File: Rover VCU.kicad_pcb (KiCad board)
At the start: 2 copper layers, 8 x 5 mm, 0 parts

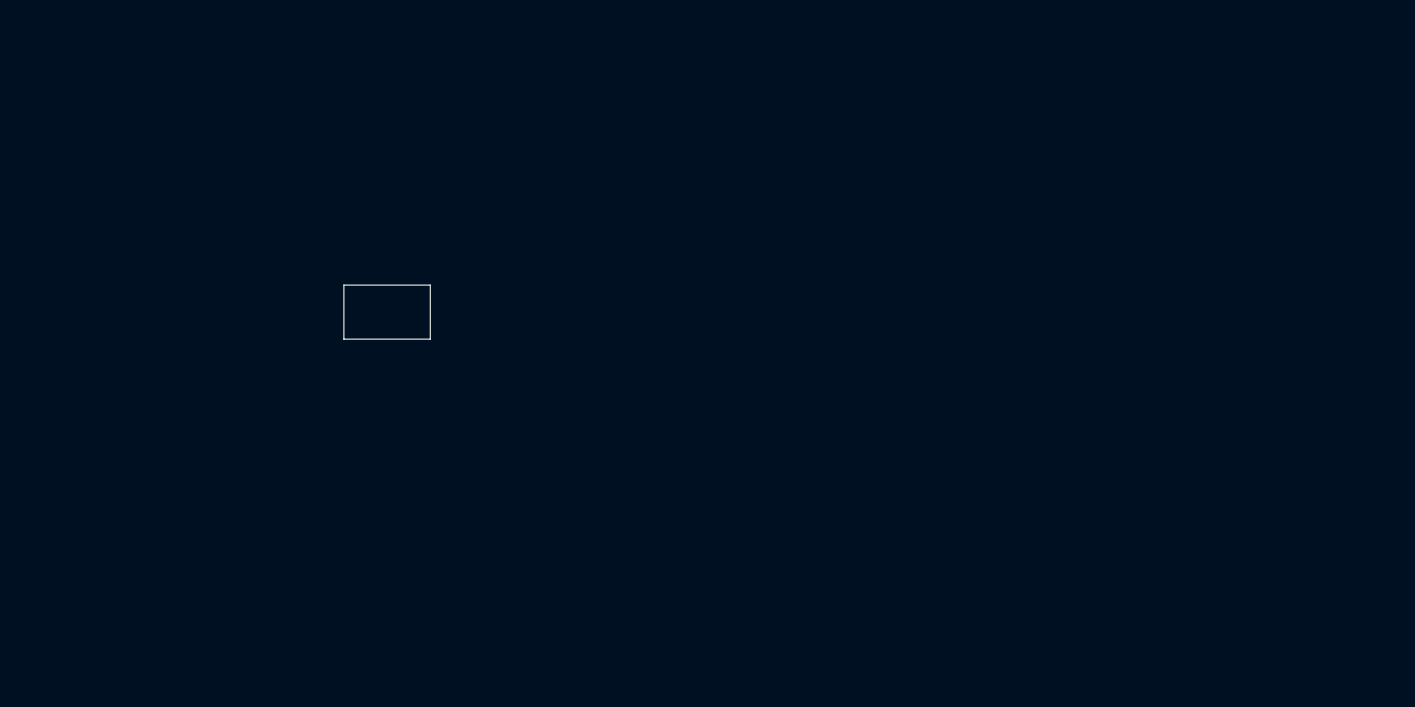
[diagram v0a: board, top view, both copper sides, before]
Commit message: feat: added MVP routing implementation
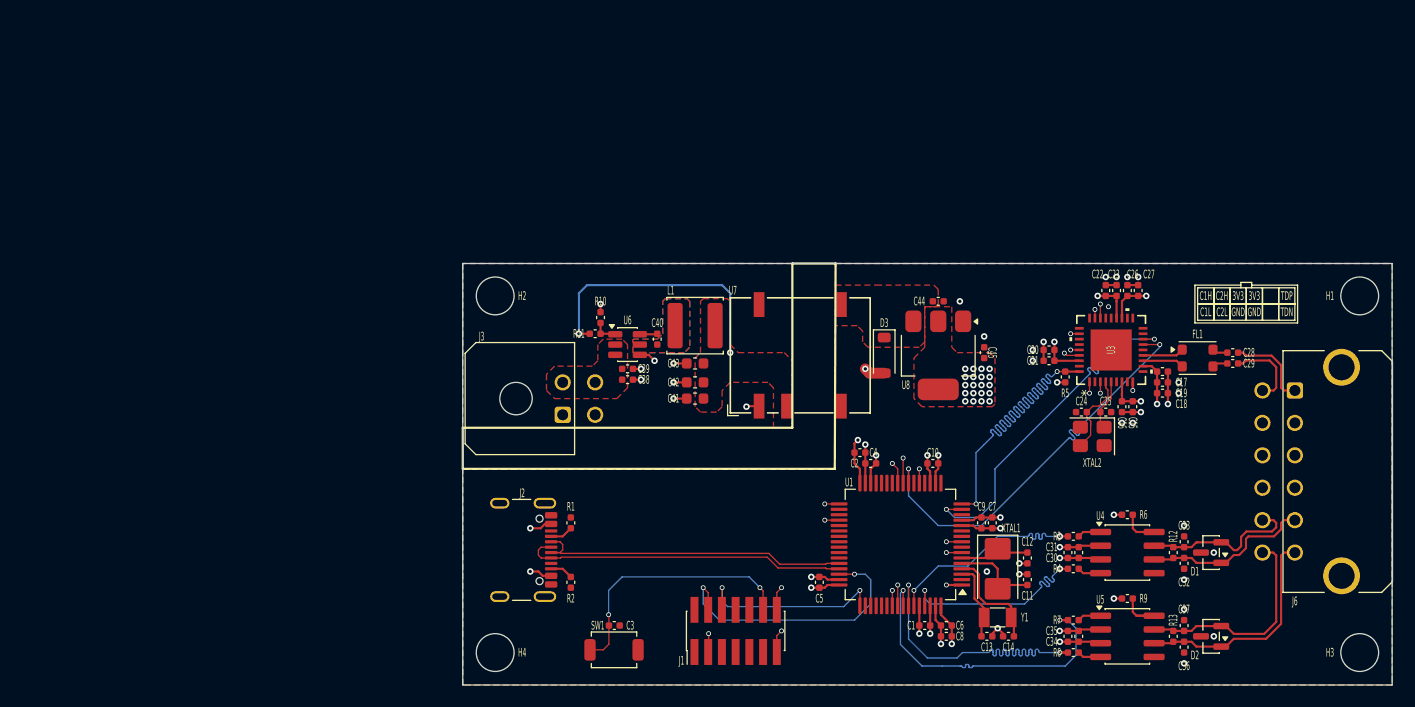
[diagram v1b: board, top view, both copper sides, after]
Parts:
- added C1: 2.2uF, chenry-footprint-lib:C_0402, F.Cu at (182.8, 128.5)
- added C10: 100nF, chenry-footprint-lib:C_0402, F.Cu at (183.5, 113.5)
- added C11: 10pF, chenry-footprint-lib:C_0402, F.Cu at (192.2, 124.2)
- added C12: 10pF, chenry-footprint-lib:C_0402, F.Cu at (192.3, 122.2)
- added C13: 6pF, chenry-footprint-lib:C_0402, F.Cu at (188.5, 129.5)
- added C14: 6pF, chenry-footprint-lib:C_0402, F.Cu at (190.5, 129.5)
- added C15: 100nF, chenry-footprint-lib:C_0402, F.Cu at (202.0, 108.2)
- added C16: 1uF, chenry-footprint-lib:C_0402, F.Cu at (201.0, 108.2)
- added C17: 10nF, chenry-footprint-lib:C_0402, F.Cu at (204.8, 105.0)
- added C18: 470nF, chenry-footprint-lib:C_0402, F.Cu at (204.8, 107.0)
- added C19: 1uF, chenry-footprint-lib:C_0402, F.Cu at (204.8, 106.0)
- added C2: 2.2uF, chenry-footprint-lib:C_0402, F.Cu at (177.8, 113.5)
- added C20: 10nF, chenry-footprint-lib:C_0402, F.Cu at (194.2, 103.0)
- added C21: 1uF, chenry-footprint-lib:C_0402, F.Cu at (194.2, 104.0)
- added C22: 470nF, chenry-footprint-lib:C_0402, F.Cu at (199.5, 97.5)
- added C23: 10nF, chenry-footprint-lib:C_0402, F.Cu at (200.5, 97.5)
- added C24: 22pF, chenry-footprint-lib:C_0402, F.Cu at (197.2, 108.8)
- added C25: 22pF, chenry-footprint-lib:C_0402, F.Cu at (199.5, 108.8)
- added C26: 100nF, chenry-footprint-lib:C_0402, F.Cu at (201.5, 97.5)
- added C27: 2.2uF, chenry-footprint-lib:C_0402, F.Cu at (202.5, 97.5)
- added C28: 100nF, chenry-footprint-lib:C_0402, F.Cu at (211.2, 104.2)
- added C29: 100nF, chenry-footprint-lib:C_0402, F.Cu at (211.2, 103.2)
- added C3: 100nF, chenry-footprint-lib:C_0402, F.Cu at (154.0, 128.5)
- added C30: 4.7uF, chenry-footprint-lib:C_0402, F.Cu at (196.0, 121.8)
- added C31: 100nF, chenry-footprint-lib:C_0402, F.Cu at (197.0, 121.8)
- added C32: 1pF, chenry-footprint-lib:C_0402, F.Cu at (206.8, 122.8)
- added C33: 1pF, chenry-footprint-lib:C_0402, F.Cu at (206.8, 120.8)
- added C34: 4.7uF, chenry-footprint-lib:C_0402, F.Cu at (196.0, 129.5)
- added C35: 100nF, chenry-footprint-lib:C_0402, F.Cu at (197.0, 129.5)
- added C36: 1pF, chenry-footprint-lib:C_0402, F.Cu at (206.8, 130.5)
- added C37: 1pF, chenry-footprint-lib:C_0402, F.Cu at (206.8, 128.5)
- added C38: 100nF, chenry-footprint-lib:C_0402, F.Cu at (155.3, 105.8)
- added C39: 1uF, chenry-footprint-lib:C_0402, F.Cu at (155.2, 104.8)
- added C4: 100nF, chenry-footprint-lib:C_0402, F.Cu at (176.8, 112.5)
- added C40: 100nF, chenry-footprint-lib:C_0402, F.Cu at (158.0, 102.0)
- added C41: 22uF, Capacitor_SMD:C_0603_1608Metric, F.Cu at (161.5, 107.5)
- added C42: 22uF, Capacitor_SMD:C_0603_1608Metric, F.Cu at (161.5, 106.0)
- added C43: 22uF, Capacitor_SMD:C_0603_1608Metric, F.Cu at (161.5, 104.2)
- added C44: 1uF, chenry-footprint-lib:C_0402, F.Cu at (184.0, 98.5)
- added C45: 1uF, chenry-footprint-lib:C_0402, F.Cu at (188.2, 103.2)
- added C5: 100nF, chenry-footprint-lib:C_0402, F.Cu at (173.0, 124.5)
- added C6: 100nF, chenry-footprint-lib:C_0402, F.Cu at (184.8, 128.5)
- added C7: 4.7uF, chenry-footprint-lib:C_0402, F.Cu at (189.0, 119.0)
- added C8: 4.7uF, chenry-footprint-lib:C_0402, F.Cu at (184.8, 129.5)
- added C9: 100nF, chenry-footprint-lib:C_0402, F.Cu at (188.0, 119.0)
- added D1: NUP2105L, Package_TO_SOT_SMD:SOT-23, F.Cu at (209.2, 121.8)
- added D2: NUP2105L, Package_TO_SOT_SMD:SOT-23, F.Cu at (209.2, 129.5)
- added D3: B5819W, Diode_SMD:D_SOD-123, F.Cu at (179.0, 103.5)
- added FL1: 9kOhm@10MHz & 10kOhm@100Mhz, Inductor_SMD:L_CommonModeChoke_Coilank_ACM3225, F.Cu at (208.0, 103.8)
- added H1: MountingHole, MountingHole:MountingHole_3.5mm, F.Cu at (223.0, 98.0)
- added H2: MountingHole, MountingHole:MountingHole_3.5mm, F.Cu at (143.0, 98.0)
- added H3: MountingHole, MountingHole:MountingHole_3.5mm, F.Cu at (223.0, 131.0)
- added H4: MountingHole, MountingHole:MountingHole_3.5mm, F.Cu at (143.0, 131.0)
- added J1: Conn_ST_STDC14, Connector_PinHeader_1.27mm:PinHeader_2x07_P1.27mm_Vertical_SMD, F.Cu at (165.2, 129.0)
- added J2: USB4105-GF-A, Connector_USB:USB_C_Receptacle_GCT_USB4105-xx-A_16P_TopMnt_Horizontal, F.Cu at (144.5, 121.5)
- added J3: 430450400, Connector_Molex:Molex_Micro-Fit_3.0_43045-0400_2x02_P3.00mm_Horizontal, F.Cu at (149.2, 109.0)
- added J6: 430451200, Connector_Molex:Molex_Micro-Fit_3.0_43045-1221_2x06-1MP_P3.00mm_Horizontal, F.Cu at (217.0, 106.8)
- added L1: 15uH, Inductor_SMD:L_Sunlord_SWPA5040S, F.Cu at (161.5, 100.8)
- added R1: 5K1, chenry-footprint-lib:R_0402, F.Cu at (150.0, 119.0)
- added R10: 10K, chenry-footprint-lib:R_0402, F.Cu at (152.8, 100.0)
- added R11: 56K, chenry-footprint-lib:R_0402, F.Cu at (152.2, 101.5)
- added R12: 120R, chenry-footprint-lib:R_0402, F.Cu at (205.8, 121.8)
- added R13: 120R, chenry-footprint-lib:R_0402, F.Cu at (205.8, 129.5)
- added R2: 5K1, chenry-footprint-lib:R_0402, F.Cu at (150.0, 124.5)
- added R3: 10K, chenry-footprint-lib:R_0402, F.Cu at (196.5, 120.2)
- added R4: 10K, chenry-footprint-lib:R_0402, F.Cu at (196.5, 123.2)
- added R5: 10K, chenry-footprint-lib:R_0402, F.Cu at (195.8, 105.5)
- added R6: 10K, chenry-footprint-lib:R_0402, F.Cu at (201.5, 118.2)
- added R7: 10K, chenry-footprint-lib:R_0402, F.Cu at (196.5, 128.0)
- added R8: 10K, chenry-footprint-lib:R_0402, F.Cu at (196.5, 131.0)
- added R9: 10K, chenry-footprint-lib:R_0402, F.Cu at (201.5, 126.0)
- added SW1: TS-1088-AR02016, Button_Switch_SMD:SW_SPST_TS-1088-xR020, F.Cu at (154.0, 130.8)
- added U1: STM32H563RITx, Package_QFP:LQFP-64_10x10mm_P0.5mm, F.Cu at (180.5, 121.0)
- added U3: DP83TC812RRHARQ1, chenry-footprint-lib:VQFN36_RHA_TEX, F.Cu at (200.0, 103.0)
- added U4: SN65HVD230, Package_SO:SOIC-8_3.9x4.9mm_P1.27mm, F.Cu at (201.5, 121.8)
- added U5: SN65HVD230, Package_SO:SOIC-8_3.9x4.9mm_P1.27mm, F.Cu at (201.5, 129.5)
- added U6: LMR51610, Package_TO_SOT_SMD:SOT-23-6, F.Cu at (155.2, 102.5)
- added U7: NXE2S0505MC, Converter_DCDC:Converter_DCDC_Murata_NXExSxxxxMC_SMD, F.Cu at (172.5, 103.5)
- added U8: NCP1117-3.3_SOT223, Package_TO_SOT_SMD:SOT-223-3_TabPin2, F.Cu at (184.0, 103.5)
- added XTAL1: 8MHz, Crystal:Crystal_SMD_5032-2Pin_5.0x3.2mm, F.Cu at (189.5, 123.2)
- added XTAL2: 25MHz, Crystal:Crystal_SMD_3225-4Pin_3.2x2.5mm, F.Cu at (198.2, 111.0)
- added Y1: 32.768kHz, Crystal:Crystal_SMD_3215-2Pin_3.2x1.5mm, F.Cu at (189.5, 127.8)
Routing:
- net /MCU/NRST: track 0.00 -> 78.3 mm, vias 0 -> 4
- net /VBUS_5V: track 0.00 -> 52.7 mm, vias 0 -> 3
- net /MCU/RMII_TXD1: track 0.00 -> 42.6 mm, vias 0 -> 2
- net /MCU/RMII_RXD1: track 0.00 -> 42.6 mm, vias 0 -> 2
- net /MCU/RMII_TXD0: track 0.00 -> 42.5 mm, vias 0 -> 2
- net /MCU/RMII_RXD0: track 0.00 -> 42.5 mm, vias 0 -> 2
- net /MCU/RMII_TX_EN: track 0.00 -> 42.5 mm, vias 0 -> 2
- net /MCU/RMII_MDC: track 0.00 -> 42.5 mm, vias 0 -> 2
- net GND: track 0.00 -> 40.5 mm, vias 0 -> 36
- net /MCU/RMII_CRS_DV: track 0.00 -> 39.8 mm, vias 0 -> 2
- net /MCU/RMII_REF_CLK: track 0.00 -> 39.7 mm, vias 0 -> 2
- net /MCU/RMII_MDIO: track 0.00 -> 39.6 mm, vias 0 -> 2
- net /MCU/CAN2_TX: track 0.00 -> 30.4 mm, vias 0 -> 2
- net /MCU/CAN2_RX: track 0.00 -> 30.4 mm, vias 0 -> 2
- net /MCU/USB_DP: track 0.00 -> 30.2 mm
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- added copper zone on F.Cu, net /VDD_3V3
- added copper zone on In2.Cu, net /VDD_3V3
- added copper zone on F.Cu, net /VDD_48V
- added copper zone on B.Cu, net GND
- added copper zone on F.Cu, net GND
- added copper zone on In1.Cu, net GND
- added copper zone on B.Cu, net GND_CHASIS
- added copper zone on F.Cu, net GND_CHASIS
- added copper zone on In1.Cu, net GND_CHASIS
- added copper zone on In2.Cu, net GND_CHASIS
- added copper zone on F.Cu, net Net-(D3-K)
- added copper zone on B.Cu, net Net-(U6-SW)
- added copper zone on F.Cu, net Net-(U6-SW)
- added copper zone on In1.Cu, net Net-(U6-SW)
- added copper zone on In2.Cu, net Net-(U6-SW)
- added copper zone on F.Cu, net Net-(U7-+VIN)
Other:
- board size 8 x 5 mm -> 86 x 39 mm
- copper layers 2 -> 4
- board text added: "3V3"
- board text added: "C1H"
- board text added: "C1L"
- board text added: "C2H"
- board text added: "C2L"
- board text added: "GND"
- board text added: "TDN"
- board text added: "TDP"

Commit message: fix: centering board on layout
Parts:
- moved C1 46.4 mm to (142.0, 106.2)
- moved C10 46.4 mm to (142.8, 91.2)
- moved C11 46.4 mm to (151.5, 102.0)
- moved C13 46.4 mm to (147.8, 107.2)
- moved C15 46.4 mm to (161.3, 86.0)
- moved C16 46.4 mm to (160.3, 86.0)
- moved C2 46.4 mm to (137.0, 91.2)
- moved C20 46.4 mm to (153.5, 80.7)
- moved C21 46.4 mm to (153.5, 81.7)
- moved C22 46.4 mm to (158.8, 75.2)
- moved C23 46.4 mm to (159.8, 75.2)
- moved C24 46.4 mm to (156.5, 86.5)
- moved C25 46.4 mm to (158.8, 86.5)
- moved C26 46.4 mm to (160.8, 75.2)
- moved C27 46.4 mm to (161.8, 75.2)
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
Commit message: chore: updating Rover
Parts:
- moved C1 8.07 mm to (145.5, 113.5)
- moved C10 8.07 mm to (146.2, 98.5)
- moved C11 8.07 mm to (155.0, 109.2)
- moved C13 8.07 mm to (151.2, 114.5)
- moved C15 8.07 mm to (164.8, 93.2)
- moved C16 8.07 mm to (163.8, 93.2)
- moved C2 8.07 mm to (140.5, 98.5)
- moved C20 8.07 mm to (157.0, 88.0)
- moved C21 8.07 mm to (157.0, 89.0)
- moved C22 8.07 mm to (162.2, 82.5)
- moved C23 8.07 mm to (163.2, 82.5)
- moved C24 8.07 mm to (160.0, 93.8)
- moved C25 8.07 mm to (162.2, 93.8)
- moved C26 8.07 mm to (164.2, 82.5)
- moved C27 8.07 mm to (165.2, 82.5)
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
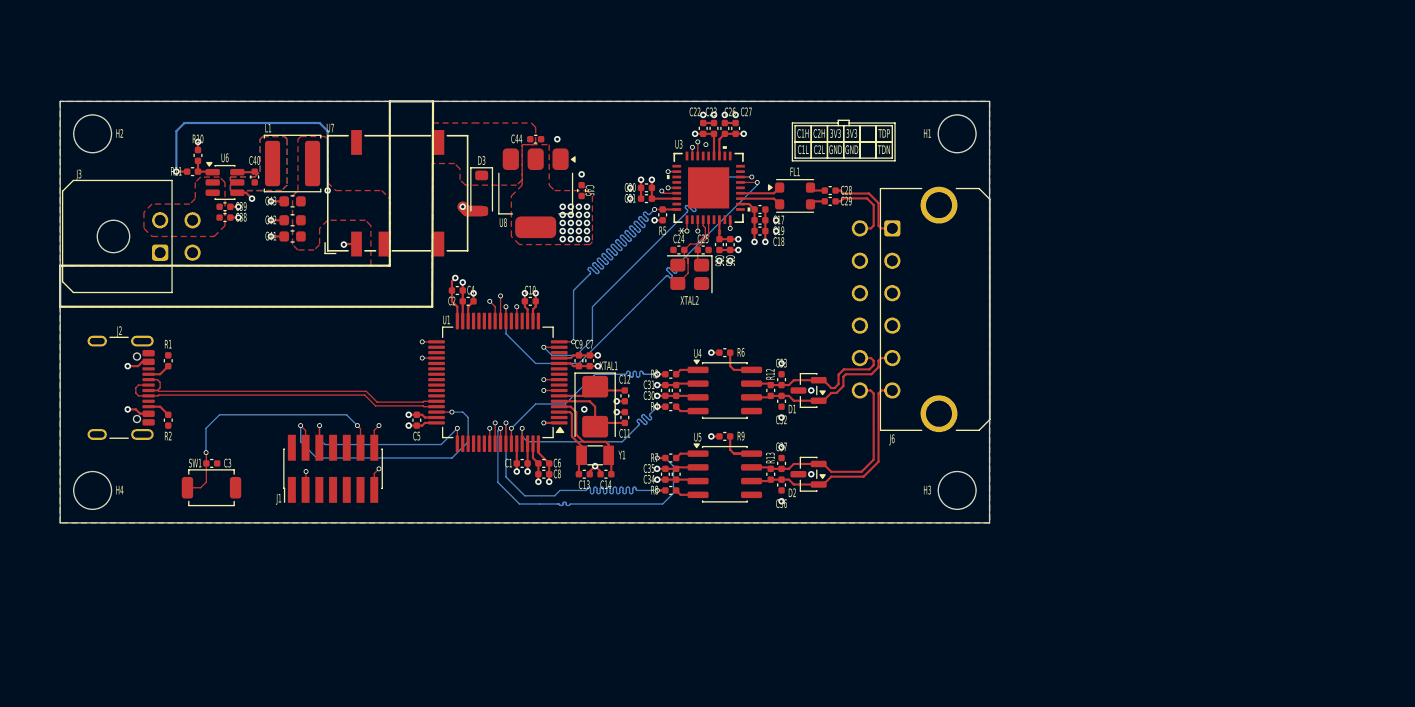
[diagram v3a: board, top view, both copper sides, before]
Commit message: fix: cleaned up DRC and ERC's for major errors
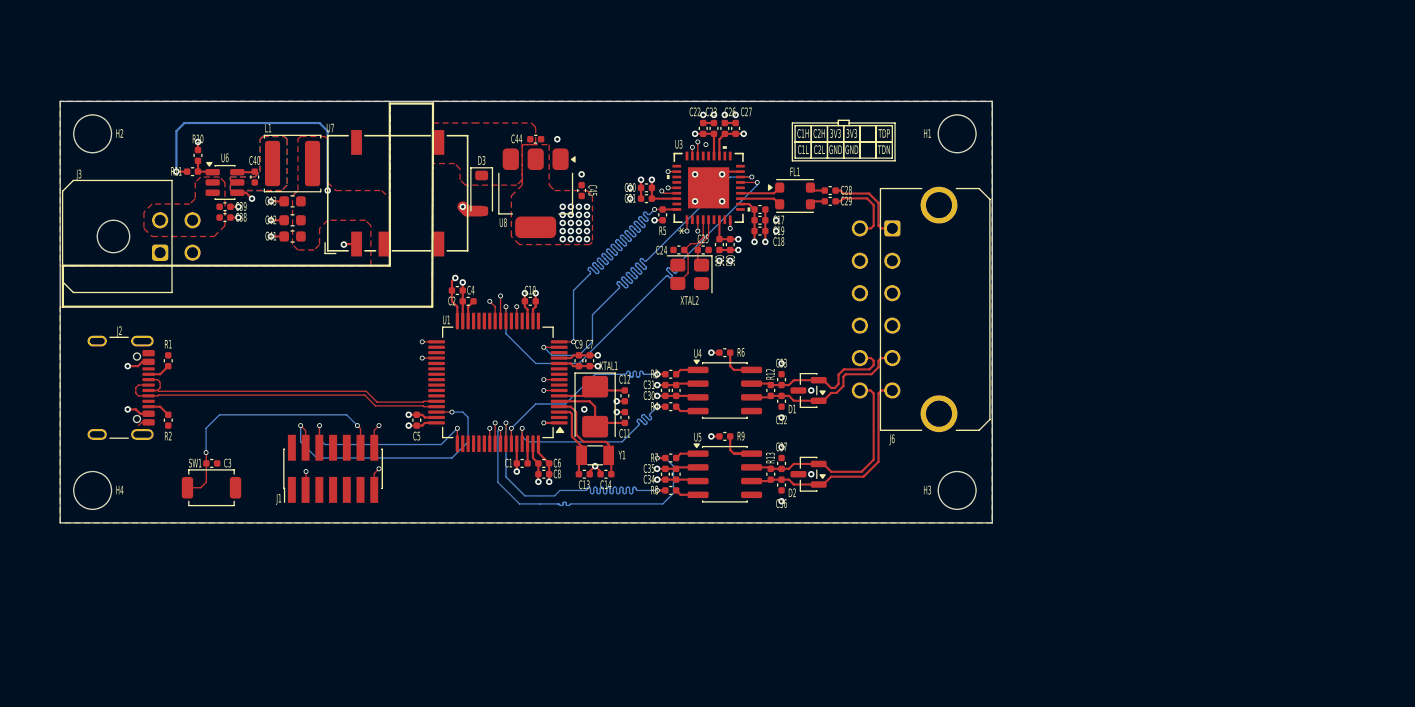
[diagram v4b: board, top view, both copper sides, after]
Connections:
- C15 pad 1: Net-(U3-VSLEEP) -> /VDD_3V3
- C16 pad 1: Net-(U3-VSLEEP) -> /VDD_3V3
- C17 pad 1: Net-(U3-VDDA) -> /VDD_3V3
- C18 pad 1: Net-(U3-VDDA) -> /VDD_3V3
- C19 pad 1: Net-(U3-VDDA) -> /VDD_3V3
- C20 pad 1: Net-(U3-VDDIO) -> /VDD_3V3
- C21 pad 1: Net-(U3-VDDIO) -> /VDD_3V3
- C22 pad 1: Net-(U3-VDDMAC) -> /VDD_3V3
- C23 pad 1: Net-(U3-VDDMAC) -> /VDD_3V3
- U3 pad 11: Net-(U3-VDDA) -> /VDD_3V3
- U3 pad 22: Net-(U3-VDDMAC) -> /VDD_3V3
- U3 pad 34: Net-(U3-VDDIO) -> /VDD_3V3
- U3 pad 7: Net-(U3-VSLEEP) -> /VDD_3V3
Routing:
- net /VDD_3V3: track 28.9 -> 44.8 mm, vias 30 -> 34
- net Net-(U3-VDDA): track 4.51 -> 0.00 mm, vias 1 -> 0
- net GND: track 40.5 -> 44.6 mm, vias 36 -> 40
- net Net-(U3-VDDIO): track 4.05 -> 0.00 mm, vias 1 -> 0
- net Net-(U3-VDDMAC): track 3.80 -> 0.00 mm, vias 1 -> 0
- net Net-(U3-VSLEEP): track 3.80 -> 0.00 mm, vias 1 -> 0
- net Net-(C1-Pad1): track 2.58 -> 1.75 mm, vias 1 -> 0
- net Net-(C2-Pad1): track 2.78 -> 2.03 mm, vias 1 -> 0
- net Net-(U3-XO): track 8.08 -> 7.50 mm
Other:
- board size 86 x 39 mm -> 86.2 x 39 mm

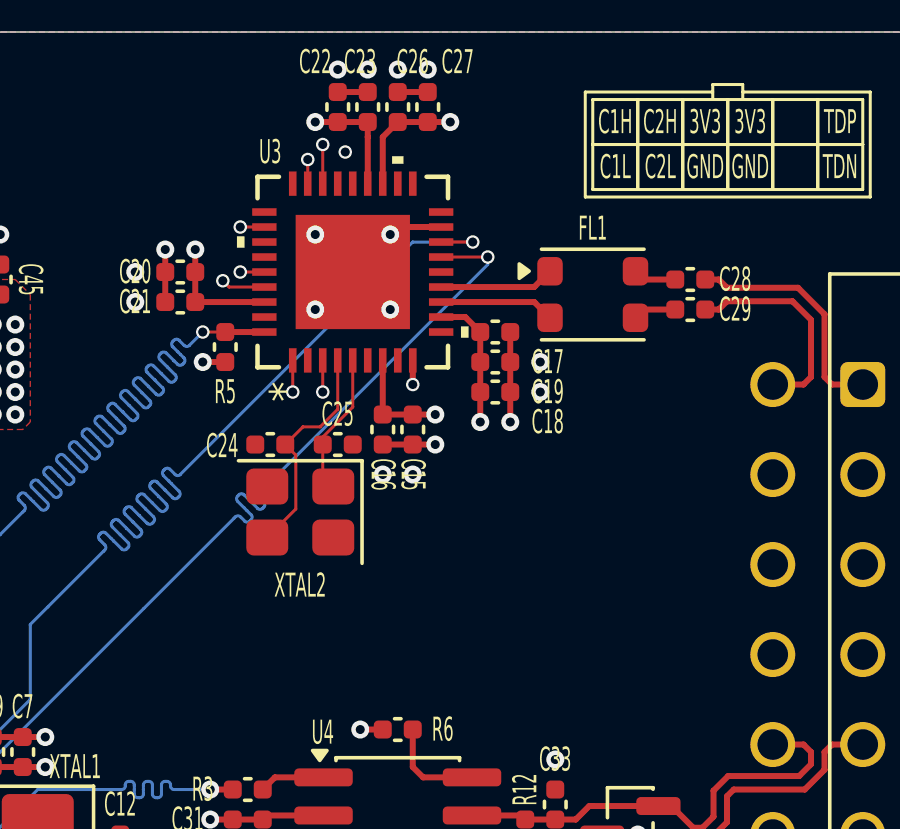
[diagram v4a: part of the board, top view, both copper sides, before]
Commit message: fix: adde more changes from excel checklist for eth phy
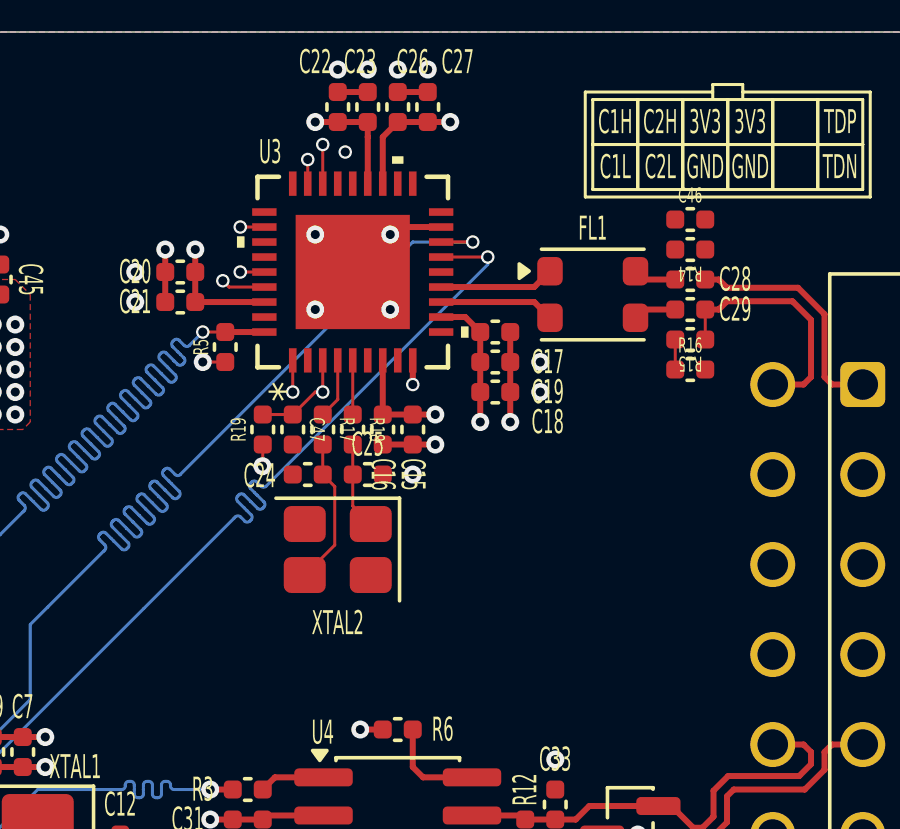
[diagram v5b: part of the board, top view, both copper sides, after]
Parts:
- added C46: 4.7uF, chenry-footprint-lib:C_0402, F.Cu at (174.0, 86.2)
- added C47: 1uF, chenry-footprint-lib:C_0402, F.Cu at (160.8, 93.2)
- added R14: 1K, chenry-footprint-lib:R_0402, F.Cu at (174.0, 87.2)
- added R15: 1K, chenry-footprint-lib:R_0402, F.Cu at (174.0, 90.2)
- added R16: 100K, chenry-footprint-lib:R_0402, F.Cu at (174.0, 91.2)
- added R17: 100R, chenry-footprint-lib:R_0402, F.Cu at (161.8, 93.2)
- added R18: 100R, chenry-footprint-lib:R_0402, F.Cu at (162.8, 93.2)
- added R19: 2K2, chenry-footprint-lib:R_0402, F.Cu at (159.8, 93.2)
- R5: value 10K -> 2K2
- moved XTAL2 1.77 mm to (162.2, 97.2)
- moved C24 1.60 mm to (161.2, 94.8)
- moved C25 1.41 mm to (163.2, 94.8)
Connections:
- C24 pad 1: Net-(U3-XO) -> Net-(C24-Pad1)
- C25 pad 1: Net-(U3-XI) -> Net-(C25-Pad1)
- U3 pad 8: unconnected-(U3-WAKE-Pad8) -> /VDD_3V3
- XTAL2 pad 1: Net-(U3-XI) -> Net-(C25-Pad1)
- XTAL2 pad 3: Net-(U3-XO) -> Net-(C24-Pad1)
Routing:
- net Net-(U3-XO): track 7.50 -> 2.01 mm
- net Net-(C24-Pad1): track 0.00 -> 4.93 mm
- net Net-(U3-XI): track 4.89 -> 1.80 mm
- net Net-(C25-Pad1): track 0.00 -> 2.90 mm
- net /MCU/NRST: track 78.3 -> 80.6 mm
- net Net-(C46-Pad1): track 0.00 -> 1.00 mm
- net /TRD_P: track 7.18 -> 8.18 mm
- net /VDD_3V3: track 44.8 -> 45.5 mm, vias 34 -> 35
- net GND: vias 40 -> 39
